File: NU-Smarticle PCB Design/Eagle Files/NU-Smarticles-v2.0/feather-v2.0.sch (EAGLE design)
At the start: 42 parts, among them CON1 12XFFCMOLEX_51281, IC1 ATMEGA328P, Q1 DMG341, SW1 KMR2, U1 MCP73831T-2ACI/OT, U2 AP2112-3.3, U3 CP2104, X1 20329, Y1 CSTCE16M0V53-R0 8MHZ

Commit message: eagle work and files added
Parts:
- removed D4, D5: YELLOW, NU-Smarticle v2:LED0603_NOOUTLINE
- removed R11: 1K, NU-Smarticle v2:RESISTOR_0603MP
- removed R16: 10K, NU-Smarticle v2:RESISTOR_0603MP
- added C12, C15: 10uF, NU-Smarticle v2:CAP_CERAMIC_0603MP
- added C13: 0.1uF, NU-Smarticle v2:CAP_CERAMIC_0603MP
- added C14: 1uF, NU-Smarticle v2:CAP_CERAMIC_0603MP
- added U$1: ADXL337, NU-Smarticle v2:ADXL337
- C1: value 0.1uF -> 1uF
- C10, C6: value 1uF -> 0.1uF
- C11, C8, C9: value 10uF -> 10nF
- C2, C3: value 0.1uF -> 10µF
- C4, C7: value 10µF -> 0.1uF
- C5: value 0.1uF -> 10uF
- D1: value ORANGE -> RED
- D3: value RED -> ORANGE
- R1, R6: value 100k -> 1K
- R10: value 1K -> 10K
- R4: value 10K -> 1K
- R5: value 100k -> 10K
- R7, R8, R9: value 1K -> 100k
- Y1: value CSTCE16M0V53-R0 8MHZ -> RESONATORMU
- renumbered CON1 to CON100
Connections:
- net XTAL1 renamed N$9
- net XTAL2 renamed N$17
- removed net D11/MOSI: IC1.PB3(MOSI/OC2), JP2.5
- removed net D12/MISO: IC1.PB4(MISO), JP2.4
- removed net N$11: R11.2
- removed net N$8: D5.A, R10.1
- removed net N$9 (its old number): D4.A, R9.1
- removed net RXLED: D5.C, U3G$1.GPIO1/RXLED
- removed net TXLED: D4.C, U3G$1.GPIO0/TXLED
- new net D11/MOSI/TXD1: CON100.P7, IC1.PB3(MOSI/OC2/TXD1), JP2.5
- new net D12/MISO/RXD1: CON100.P8, IC1.PB4(MISO/RXD1), JP2.4
- new net N$13: U$1.VS@1
- new net N$14: U$1.GND@2
- new net N$15: U$1.GND@1
- new net N$16: U$1.ST
- net 3.3V: now also C10.1, C12.1, C5.1, C6.2, C7.2, R5.2, U$1.VS@2; no longer C2.2, C5.2, C8.1, C9.1, R3.2
- net A4/SDA: now also C11.1, U$1.ZOUT
- net A5/SCL: now also C9.1, U$1.YOUT
- net A6: now also R8.1, R9.2; no longer R5.1, R6.2
- net A7: now also C8.1, U$1.XOUT
- net AREF: now also C13.2; no longer C3.2
- net D0/RX: now also IC1.PD0(RXD0), R4.1; no longer IC1.PD0(RXD), R7.1
- net D1/TX: now also IC1.PD1(TXD0); no longer IC1.PD1(TXD)
- net D10: now also CON100.P9; no longer CON100.P0
- net D13/SCK: now also R1.1; no longer R8.1
- net D2: no longer CON100.P7
- net D3: no longer CON100.P8
- net D4: no longer CON100.P9
- net D7: now also J2.1; no longer J1.1
- net D9: now also CON100.P0
- net DTR: now also C4.1; no longer C1.1
- net GND: now also C1.1, C12.2, C13.1, C14.2, C15.2, C2.2, C3.2, C5.2, C7.1, D1.C, R10.1, R2.2, R3.1, R7.1, R9.1; no longer C2.1, C3.1, C4.2, C5.1, C7.2, D3.C, R1.1, R16.1, R4.1, R6.1
- net N$1: now also D3.C, R6.1; no longer D1.C, R2.1
- net N$10: now also C14.1; no longer C10.1
- net N$12: now also J1.1, R2.1; no longer J2.1, R11.1
- net N$3: now also R6.2; no longer R2.2
- net N$4: now also R3.2; no longer R4.2
- net N$41: now also C15.1; no longer C11.1
- net N$5: now also D1.A, R1.2; no longer D3.A, R8.2
- net N$7: now also R10.2; no longer R16.2
- net PWR_SLCT: now also C3.1; no longer C4.1
- net RESET: now also C4.2, R5.1; no longer C1.2, R3.1
- net RXD: now also R4.2; no longer R7.2
- net VBAT: now also C2.1, R8.2; no longer C7.1, R5.2
- net VBUS: now also C1.2, D3.A, R7.2; no longer C6.2, D1.A, R1.2, R10.2, R9.2
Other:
- moved on the sheet: C1, C2, C3, C4, C5, C6, C7, D1, D3, J1, J2, R1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

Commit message: update inventory, eagle
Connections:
- removed net N$13: U$1.VS@1
- removed net N$14: U$1.GND@2
- removed net N$15: U$1.GND@1
- net 3.3V: now also U$1.VS@1
- net GND: now also U$1.GND@1, U$1.GND@2
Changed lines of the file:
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@@
 <pinref part="U$1" gate="G$1" pin="VS@2"/>
 <wire x1="20.32" y1="-5.08" x2="15.24" y2="-5.08" width="0.1524" layer="91"/>
-<wire x1="15.24" y1="-5.08" x2="15.24" y2="2.54" width="0.1524" layer="91"/>
+<wire x1="15.24" y1="-5.08" x2="15.24" y2="-2.54" width="0.1524" layer="91"/>
 <pinref part="PWR1" gate="G$1" pin="3.3V"/>
 <pinref part="C10" gate="G$1" pin="1"/>
+<wire x1="15.24" y1="-2.54" x2="15.24" y2="2.54" width="0.1524" layer="91"/>
 <wire x1="7.62" y1="-2.54" x2="7.62" y2="2.54" width="0.1524" layer="91"/>
 <wire x1="7.62" y1="2.54" x2="15.24" y2="2.54" width="0.1524" layer="91"/>
 <junction x="15.24" y="2.54"/>
+<pinref part="U$1" gate="G$1" pin="VS@1"/>
+<wire x1="20.32" y1="-2.54" x2="15.24" y2="-2.54" width="0.1524" layer="91"/>
+<junction x="15.24" y="-2.54"/>
 </segment>
 </net>
@@
 <pinref part="GND24" gate="G$1" pin="GND"/>
 <wire x1="7.62" y1="-18.034" x2="15.24" y2="-18.034" width="0.1524" layer="91"/>
+<pinref part="U$1" gate="G$1" pin="GND@1"/>
+<wire x1="20.32" y1="-10.16" x2="15.24" y2="-10.16" width="0.1524" layer="91"/>
+<wire x1="15.24" y1="-10.16" x2="15.24" y2="-12.7" width="0.1524" layer="91"/>
+<junction x="15.24" y="-18.034"/>
+<pinref part="U$1" gate="G$1" pin="GND@2"/>
+<wire x1="15.24" y1="-12.7" x2="15.24" y2="-18.034" width="0.1524" layer="91"/>
+<wire x1="20.32" y1="-12.7" x2="15.24" y2="-12.7" width="0.1524" layer="91"/>
+<junction x="15.24" y="-12.7"/>
 </segment>
 <segment>
@@
 </segment>
 </net>
-<net name="N$13" class="0">
-<segment>
-<pinref part="U$1" gate="G$1" pin="VS@1"/>
-<wire x1="20.32" y1="-2.54" x2="15.24" y2="-2.54" width="0.1524" layer="91"/>
-</segment>
-</net>
-<net name="N$14" class="0">
-<segment>
-<pinref part="U$1" gate="G$1" pin="GND@2"/>
-<wire x1="20.32" y1="-12.7" x2="15.24" y2="-12.7" width="0.1524" layer="91"/>
-</segment>
-</net>
-<net name="N$15" class="0">
-<segment>
-<pinref part="U$1" gate="G$1" pin="GND@1"/>
-<wire x1="20.32" y1="-10.16" x2="15.24" y2="-10.16" width="0.1524" layer="91"/>
-<wire x1="15.24" y1="-10.16" x2="15.24" y2="-17.78" width="0.1524" layer="91"/>
-</segment>
-</net>

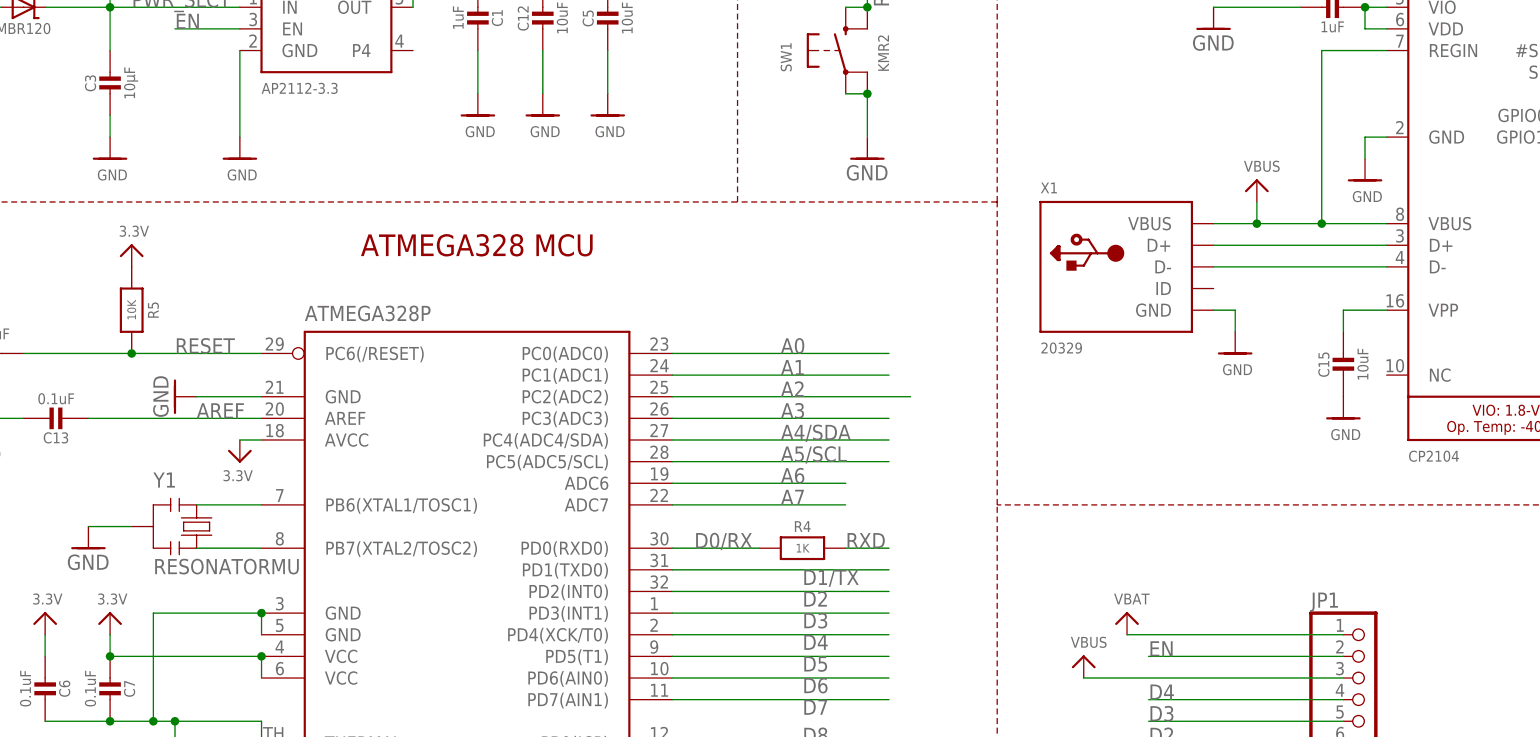
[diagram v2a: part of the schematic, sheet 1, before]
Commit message: delete cam outputs
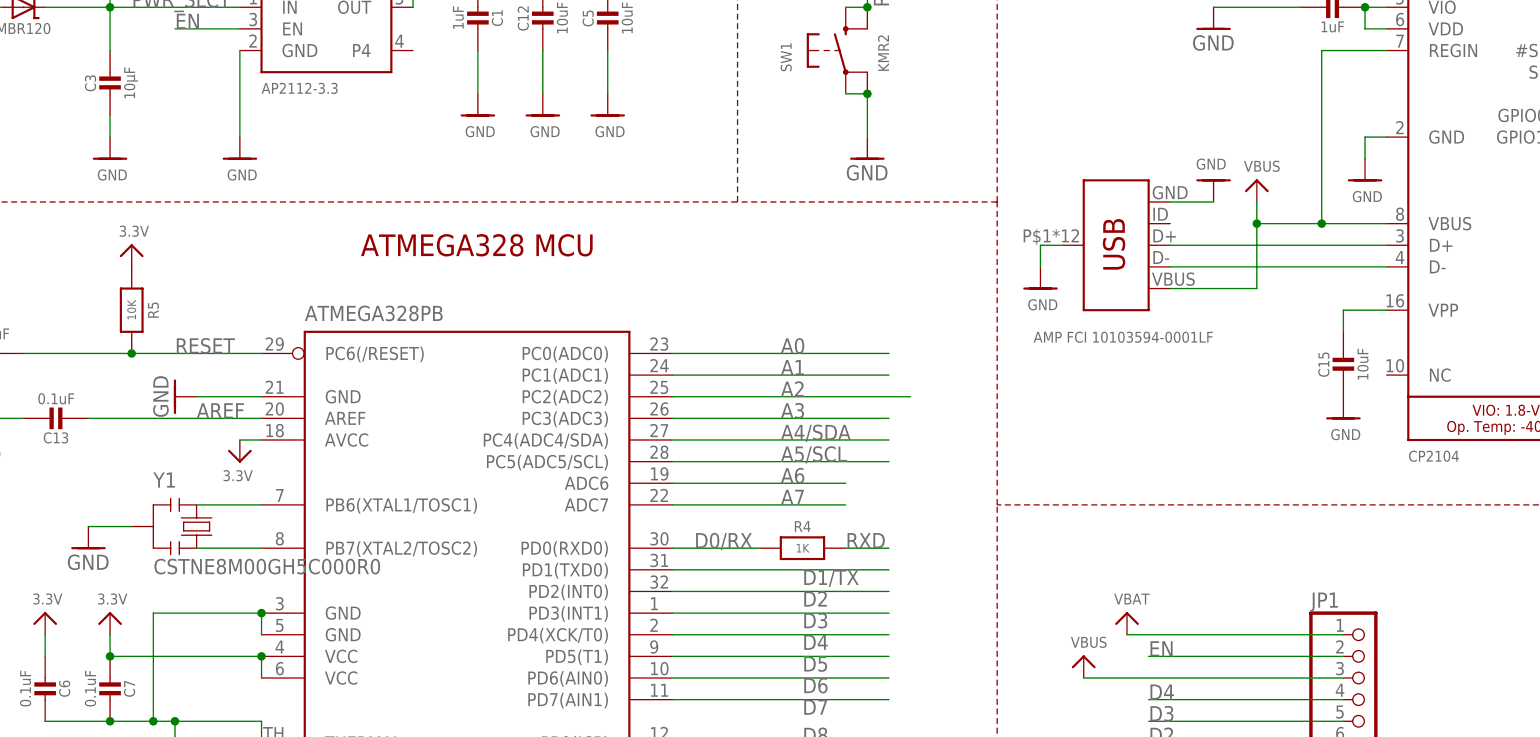
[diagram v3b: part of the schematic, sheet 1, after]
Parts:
- IC1: value ATMEGA328P -> ATMEGA328PB
- X1: value 20329 -> AMP FCI 10103594-0001LF; device NU-Smarticle v2:USB_MICRO_20329_V2 -> NU-Smarticle v2:USB_MICRO-B_HALF_PTH
- Y1: value RESONATORMU -> CSTNE8M00GH5C000R0
- renumbered U$1 to U4
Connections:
- net GND: now also X1.SHIELD
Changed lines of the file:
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@@
 <part name="PWR9" library="NU-Smarticle v2" deviceset="3.3V" device=""/>
 <part name="U3" library="NU-Smarticle v2" deviceset="CP2104" device="" value="CP2104"/>
-<part name="X1" library="NU-Smarticle v2" deviceset="USB" device="_MICRO_20329_V2" value="20329"/>
+<part name="X1" library="NU-Smarticle v2" deviceset="USB_MICRO-B" device="_HALF_PTH" package3d_urn="urn:adsk.eagle:package:38241/1" value="AMP FCI 10103594-0001LF"/>
 <part name="GND18" library="NU-Smarticle v2" deviceset="GND" device=""/>
 <part name="GND20" library="NU-Smarticle v2" deviceset="GND" device=""/>
@@
 <part name="C6" library="NU-Smarticle v2" deviceset="CAP_CERAMIC" device="_0603MP" value="0.1uF"/>
 <part name="R5" library="NU-Smarticle v2" deviceset="RESISTOR" device="_0603MP" value="10K"/>
-<part name="IC1" library="NU-Smarticle v2" deviceset="MEGA8-MI" device="" value="ATMEGA328P"/>
+<part name="IC1" library="NU-Smarticle v2" deviceset="MEGA8-MI" device="" value="ATMEGA328PB"/>
 <part name="GND6" library="NU-Smarticle v2" deviceset="GND" device=""/>
 <part name="PWR7" library="NU-Smarticle v2" deviceset="3.3V" device=""/>
@@
 <part name="R10" library="NU-Smarticle v2" deviceset="RESISTOR" device="_0603MP" value="10K"/>
 <part name="GND1" library="NU-Smarticle v2" deviceset="GND" device=""/>
-<part name="U$1" library="NU-Smarticle v2" deviceset="ADXL337" device=""/>
+<part name="U4" library="NU-Smarticle v2" deviceset="ADXL337" device=""/>
 <part name="PWR1" library="NU-Smarticle v2" deviceset="3.3V" device=""/>
 <part name="GND24" library="NU-Smarticle v2" deviceset="GND" device=""/>
@@
 <part name="C11" library="NU-Smarticle v2" deviceset="CAP_CERAMIC" device="_0603MP" value="10nF"/>
 <part name="C10" library="NU-Smarticle v2" deviceset="CAP_CERAMIC" device="_0603MP" value="0.1uF"/>
-<part name="Y1" library="NU-Smarticle v2" deviceset="RESONATOR" device="MU"/>
+<part name="Y1" library="NU-Smarticle v2" deviceset="RESONATOR" device="MU" value="CSTNE8M00GH5C000R0"/>
+<part name="GND30" library="NU-Smarticle v2" deviceset="GND" device=""/>
 </parts>
 <sheets>
@@
 <attribute name="VALUE" x="190.5" y="101.6" size="1.27" layer="96"/>
 </instance>
-<instance part="X1" gate="G$1" x="157.48" y="124.46" smashed="yes">
-<attribute name="NAME" x="147.32" y="133.096" size="1.27" layer="95"/>
-<attribute name="VALUE" x="147.32" y="114.3" size="1.27" layer="96"/>
-</instance>
-<instance part="GND18" gate="G$1" x="170.18" y="114.3" smashed="yes">
-<attribute name="VALUE" x="168.656" y="111.76" size="1.27" layer="96"/>
+<instance part="X1" gate="G$1" x="157.48" y="127" smashed="yes" rot="R180">
+<attribute name="VALUE" x="167.64" y="116.84" size="1.27" layer="96" rot="R180"/>
+</instance>
+<instance part="GND18" gate="G$1" x="167.64" y="134.62" smashed="yes" rot="R180">
+<attribute name="VALUE" x="169.164" y="137.16" size="1.27" layer="96" rot="R180"/>
 </instance>
 <instance part="GND20" gate="G$1" x="185.42" y="134.62" smashed="yes">
@@
 <attribute name="VALUE" x="43.18" y="88.392" size="1.778" layer="96"/>
 </instance>
+<instance part="GND30" gate="G$1" x="147.32" y="121.92" smashed="yes">
+<attribute name="VALUE" x="145.796" y="119.38" size="1.27" layer="96"/>
+</instance>
 </instances>
 <busses>
@@
 <pinref part="X1" gate="G$1" pin="GND"/>
 <pinref part="GND18" gate="G$1" pin="GND"/>
-<wire x1="167.64" y1="119.38" x2="170.18" y2="119.38" width="0.1524" layer="91"/>
-<wire x1="170.18" y1="119.38" x2="170.18" y2="116.84" width="0.1524" layer="91"/>
+<wire x1="162.56" y1="132.08" x2="167.64" y2="132.08" width="0.1524" layer="91"/>
 </segment>
 <segment>
@@
 <wire x1="35.56" y1="93.98" x2="40.64" y2="93.98" width="0.1524" layer="91"/>
 </segment>
+<segment>
+<pinref part="X1" gate="G$1" pin="SHIELD"/>
+<wire x1="149.86" y1="127" x2="147.32" y2="127" width="0.1524" layer="91"/>
+<wire x1="147.32" y1="127" x2="147.32" y2="124.46" width="0.1524" layer="91"/>
+<pinref part="GND30" gate="G$1" pin="GND"/>
+</segment>
 </net>
 <net name="VBUS" class="0">
@@
 </segment>
 <segment>
-<pinref part="X1" gate="G$1" pin="VBUS"/>
 <pinref part="U3" gate="G$1" pin="VBUS"/>
-<wire x1="167.64" y1="129.54" x2="172.72" y2="129.54" width="0.1524" layer="91"/>
 <wire x1="172.72" y1="129.54" x2="180.34" y2="129.54" width="0.1524" layer="91"/>
 <pinref part="PWR17" gate="G$1" pin="VBUS"/>
 <wire x1="180.34" y1="129.54" x2="187.96" y2="129.54" width="0.1524" layer="91"/>
 <wire x1="172.72" y1="129.54" x2="172.72" y2="132.08" width="0.1524" layer="91"/>
-<junction x="172.72" y="129.54"/>
 <pinref part="U3" gate="G$1" pin="REGIN"/>
 <wire x1="187.96" y1="149.86" x2="180.34" y2="149.86" width="0.1524" layer="91"/>
 <wire x1="180.34" y1="149.86" x2="180.34" y2="129.54" width="0.1524" layer="91"/>
 <junction x="180.34" y="129.54"/>
+<pinref part="X1" gate="G$1" pin="VBUS"/>
+<wire x1="162.56" y1="121.92" x2="172.72" y2="121.92" width="0.1524" layer="91"/>
+<wire x1="172.72" y1="121.92" x2="172.72" y2="129.54" width="0.1524" layer="91"/>
+<junction x="172.72" y="129.54"/>
 </segment>
 <segment>
@@
 <pinref part="X1" gate="G$1" pin="D+"/>
 <pinref part="U3" gate="G$1" pin="D+"/>
-<wire x1="167.64" y1="127" x2="187.96" y2="127" width="0.1524" layer="91"/>
+<wire x1="162.56" y1="127" x2="187.96" y2="127" width="0.1524" layer="91"/>
 </segment>
 </net>
@@
 <pinref part="X1" gate="G$1" pin="D-"/>
 <pinref part="U3" gate="G$1" pin="D-"/>
-<wire x1="167.64" y1="124.46" x2="187.96" y2="124.46" width="0.1524" layer="91"/>
+<wire x1="162.56" y1="124.46" x2="187.96" y2="124.46" width="0.1524" layer="91"/>
 </segment>
 </net>
@@
 <attribute name="VALUE" x="30.48" y="19.812" size="1.778" layer="96" align="top-center"/>
 </instance>
-<instance part="U$1" gate="G$1" x="33.02" y="-7.62" smashed="yes">
+<instance part="U4" gate="G$1" x="33.02" y="-7.62" smashed="yes">
 <attribute name="NAME" x="30.48" y="2.54" size="1.778" layer="95" rot="R180"/>
 <attribute name="VALUE" x="22.86" y="-17.78" size="1.778" layer="96"/>
@@
 </segment>
 <segment>
-<pinref part="U$1" gate="G$1" pin="VS@2"/>
+<pinref part="U4" gate="G$1" pin="VS@2"/>
 <wire x1="20.32" y1="-5.08" x2="15.24" y2="-5.08" width="0.1524" layer="91"/>
 <wire x1="15.24" y1="-5.08" x2="15.24" y2="-2.54" width="0.1524" layer="91"/>
@@
 <wire x1="7.62" y1="2.54" x2="15.24" y2="2.54" width="0.1524" layer="91"/>
 <junction x="15.24" y="2.54"/>
-<pinref part="U$1" gate="G$1" pin="VS@1"/>
+<pinref part="U4" gate="G$1" pin="VS@1"/>
 <wire x1="20.32" y1="-2.54" x2="15.24" y2="-2.54" width="0.1524" layer="91"/>
 <junction x="15.24" y="-2.54"/>
@@
 <pinref part="GND24" gate="G$1" pin="GND"/>
 <wire x1="7.62" y1="-18.034" x2="15.24" y2="-18.034" width="0.1524" layer="91"/>
-<pinref part="U$1" gate="G$1" pin="GND@1"/>
+<pinref part="U4" gate="G$1" pin="GND@1"/>
 <wire x1="20.32" y1="-10.16" x2="15.24" y2="-10.16" width="0.1524" layer="91"/>
 <wire x1="15.24" y1="-10.16" x2="15.24" y2="-12.7" width="0.1524" layer="91"/>
 <junction x="15.24" y="-18.034"/>
-<pinref part="U$1" gate="G$1" pin="GND@2"/>
+<pinref part="U4" gate="G$1" pin="GND@2"/>
 <wire x1="15.24" y1="-12.7" x2="15.24" y2="-18.034" width="0.1524" layer="91"/>
 <wire x1="20.32" y1="-12.7" x2="15.24" y2="-12.7" width="0.1524" layer="91"/>
@@
 <net name="N$16" class="0">
 <segment>
-<pinref part="U$1" gate="G$1" pin="ST"/>
+<pinref part="U4" gate="G$1" pin="ST"/>
 <wire x1="45.72" y1="-12.7" x2="48.26" y2="-12.7" width="0.1524" layer="91"/>
 <wire x1="48.26" y1="-12.7" x2="48.26" y2="-15.24" width="0.1524" layer="91"/>
@@
 <net name="A7" class="0">
 <segment>
-<pinref part="U$1" gate="G$1" pin="XOUT"/>
+<pinref part="U4" gate="G$1" pin="XOUT"/>
 <wire x1="45.72" y1="-2.54" x2="50.8" y2="-2.54" width="0.1524" layer="91"/>
 <label x="48.26" y="-2.54" size="1.778" layer="95"/>
@@
 <net name="A5/SCL" class="0">
 <segment>
-<pinref part="U$1" gate="G$1" pin="YOUT"/>
+<pinref part="U4" gate="G$1" pin="YOUT"/>
 <wire x1="45.72" y1="-5.08" x2="50.8" y2="-5.08" width="0.1524" layer="91"/>
 <label x="48.26" y="-5.08" size="1.778" layer="95"/>
@@
 <net name="A4/SDA" class="0">
 <segment>
-<pinref part="U$1" gate="G$1" pin="ZOUT"/>
+<pinref part="U4" gate="G$1" pin="ZOUT"/>
 <wire x1="45.72" y1="-7.62" x2="50.8" y2="-7.62" width="0.1524" layer="91"/>
 <label x="48.26" y="-7.62" size="1.778" layer="95"/>
